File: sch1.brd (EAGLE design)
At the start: 108.9 x 88.9 mm, 44 parts, among them K1 351, K2 351, K3 351, K4 351, K5 351, K6 351

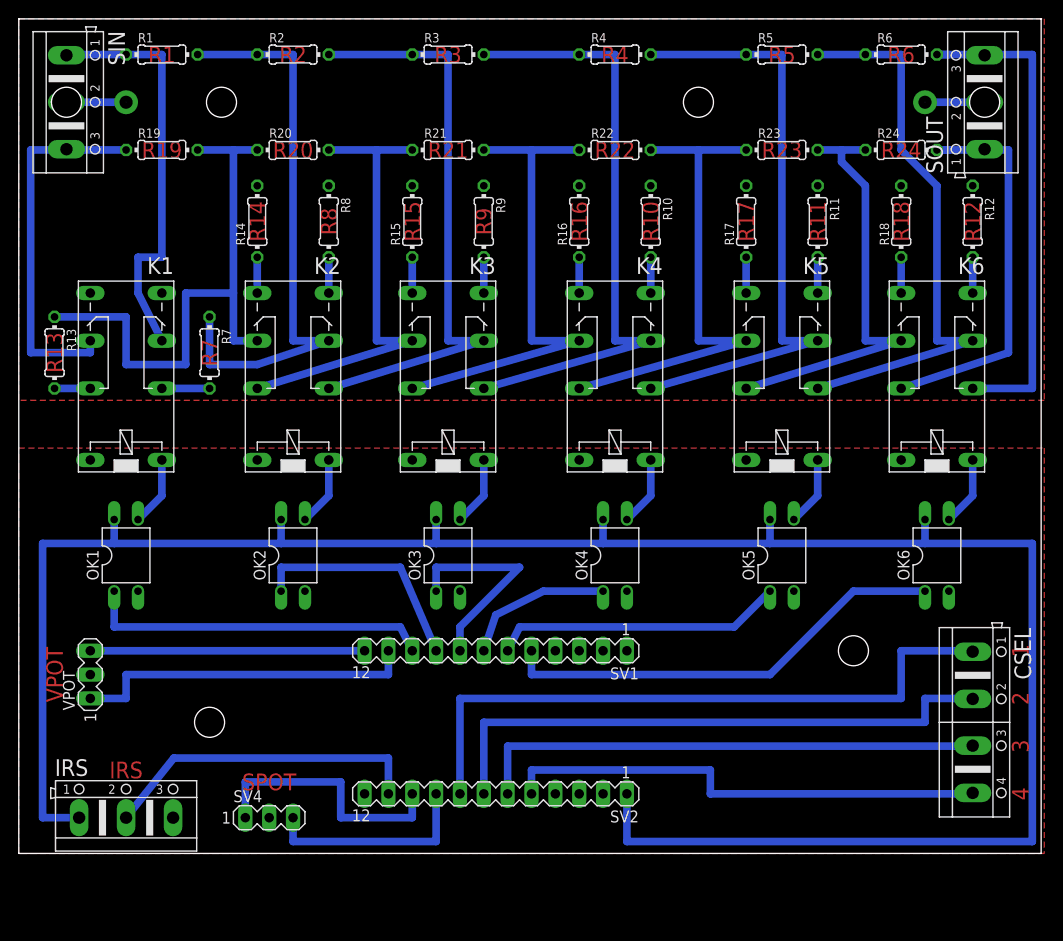
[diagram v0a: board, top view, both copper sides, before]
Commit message: added ground fill on bottom
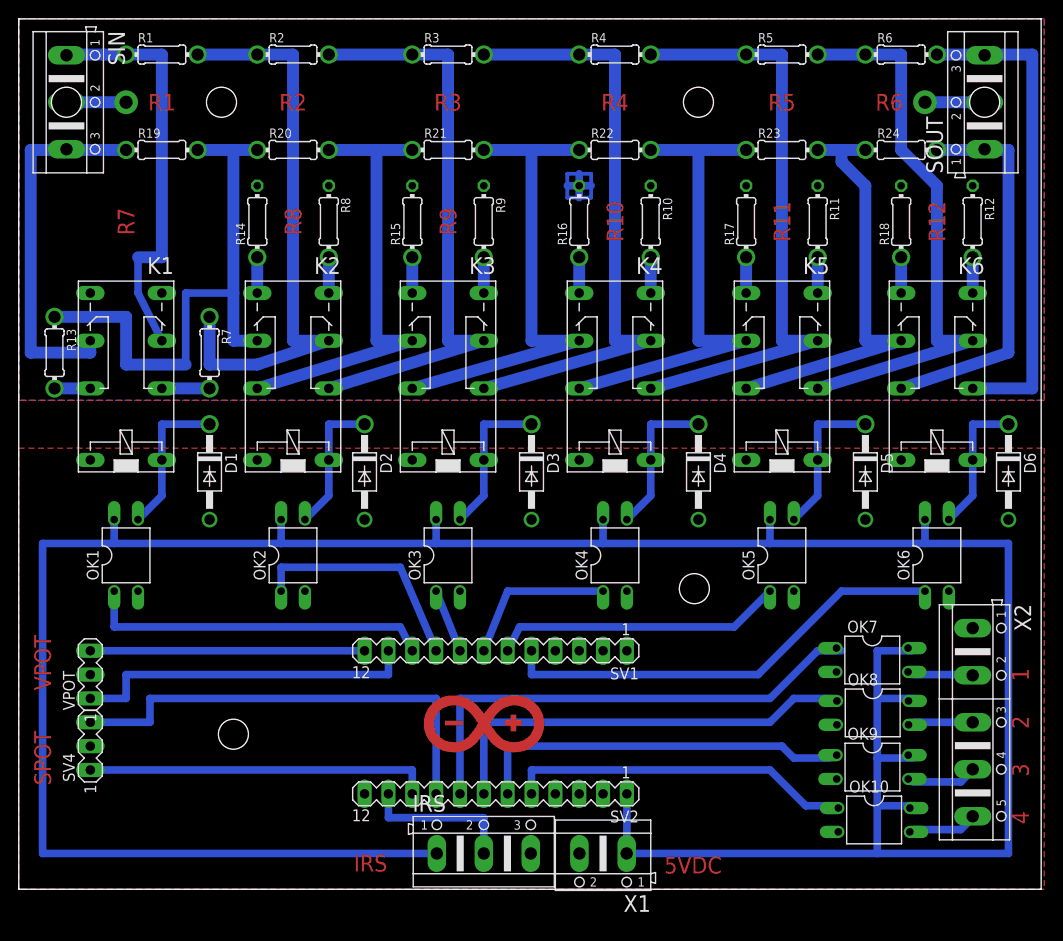
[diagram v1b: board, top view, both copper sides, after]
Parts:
- removed CSEL: (no value), con-ptr500:AK500/4
- added D1, D2, D3, D4, D5, D6: 1N4004, diode:DO41-10
- added OK10, OK7, OK8, OK9: LTV816, optocoupler:DIL04
- added X1: (no value), con-ptr500:AK500/2
- added X2: (no value), con-ptr500:AK500/5
- moved IRS 38.3 mm to (48.3, -3.81)
- moved SV4 20.5 mm to (6.35, 7.62), turned to 90 degrees
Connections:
- new net N$93: OK7.3, X2.2
- new net N$94: OK8.3, X2.3
- new net N$95: OK9.3, X2.4
- new net N$96: OK10.3, X2.5
- net GNDD: now also D1.A, D2.A, D3.A, D4.A, D5.A, D6.A, OK10.2, OK7.2, OK8.2, OK9.2, X1.2, X2.1
- net N$21: now also OK7.1; no longer CSEL.1
- net N$23: now also D1.C
- net N$24: now also D2.C
- net N$25: now also D3.C
- net N$26: now also D4.C
- net N$27: now also D5.C
- net N$33: now also D6.C
- net N$44: now also OK8.1; no longer CSEL.2
- net N$45: now also OK9.1; no longer CSEL.3
- net N$46: now also OK10.1; no longer CSEL.4
- net N$50: now also OK10.4, OK7.4, OK8.4, OK9.4, X1.1
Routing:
- net N$50: track 233.7 -> 309.9 mm
- net N$43: track 22.9 -> 49.5 mm
- net N$49: track 34.8 -> 16.5 mm
- net N$21: track 69.8 -> 52.9 mm
- net N$44: track 62.2 -> 45.5 mm
- net N$46: track 52.1 -> 35.9 mm
- net N$39: track 23.0 -> 6.84 mm
- net N$110: track 0.00 -> 15.2 mm
- net N$45: track 54.6 -> 39.9 mm
- net N$27: track 7.40 -> 16.3 mm
- net N$25: track 7.40 -> 16.3 mm
- net N$42: track 27.9 -> 36.8 mm
- net N$26: track 7.40 -> 16.3 mm
- net N$23: track 7.40 -> 16.3 mm
- net N$33: track 7.40 -> 15.0 mm
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- added copper zone on layer 16, net N$109
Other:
- board size 108.9 x 88.9 mm -> 108.9 x 92.7 mm
- board text added: "5VDC"
- board text added: "C:/Users/l0014/Desktop/Arduino_Logo.bmp"
- board text removed: "R13"
- board text removed: "R14"
- board text removed: "R15"
- board text removed: "R16"
- board text removed: "R17"
- board text removed: "R18"
- board text removed: "R19"
- board text removed: "R20"
- board text removed: "R21"
- board text removed: "R22"
- board text removed: "R23"
- board text removed: "R24"
